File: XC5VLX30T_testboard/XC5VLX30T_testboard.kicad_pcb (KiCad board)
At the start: 4 copper layers, 19 parts, among them J1 Conn_01x35_Pin, J2 Conn_01x35_Pin, J3 Conn_01x35_Pin, J4 Conn_01x35_Pin, J5 Conn_01x35_Pin, J6 Conn_01x35_Pin, J7 Conn_01x35_Pin, J8 Conn_01x35_Pin, U1 XC5VLX30T-1FFG665C, X1 SG-5032CCN

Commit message: a
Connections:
- U1 pad AA16: unconnected-(U1F-IO_L4P_13-PadU26) -> VCCO
- U1 pad AA6: unconnected-(U1F-IO_L4P_13-PadU26) -> VCCO
- U1 pad AB13: unconnected-(U1F-IO_L4P_13-PadU26) -> VCCO
- U1 pad AB23: unconnected-(U1F-IO_L4P_13-PadU26) -> VCCO
- U1 pad AC10: unconnected-(U1F-IO_L4P_13-PadU26) -> VCCO
- U1 pad AC20: unconnected-(U1F-IO_L4P_13-PadU26) -> VCCO
- U1 pad B13: unconnected-(U1F-IO_L4P_13-PadU26) -> VCCO
- U1 pad B23: unconnected-(U1F-IO_L4P_13-PadU26) -> VCCO
- U1 pad C10: unconnected-(U1F-IO_L4P_13-PadU26) -> VCCO
- U1 pad C23: unconnected-(U1F-IO_L4P_13-PadU26) -> unconnected-(U1C-IO_L15N_15-PadC23)
- U1 pad D17: unconnected-(U1F-IO_L4P_13-PadU26) -> VCCO
- U1 pad D23: unconnected-(U1F-IO_L4P_13-PadU26) -> unconnected-(U1D-IO_L12P_VRN_15-PadD23)
- U1 pad D7: unconnected-(U1F-IO_L4P_13-PadU26) -> VCCO
- U1 pad E14: unconnected-(U1F-IO_L4P_13-PadU26) -> VCCO
- U1 pad E24: unconnected-(U1F-IO_L4P_13-PadU26) -> VCCO
- U1 pad F11: unconnected-(U1F-IO_L4P_13-PadU26) -> VCCO
- U1 pad F21: unconnected-(U1F-IO_L4P_13-PadU26) -> VCCO
- U1 pad G18: unconnected-(U1F-IO_L4P_13-PadU26) -> VCCO
- U1 pad G8: unconnected-(U1F-IO_L4P_13-PadU26) -> VCCO
- U1 pad H25: unconnected-(U1F-IO_L4P_13-PadU26) -> VCCO
- U1 pad H5: unconnected-(U1F-IO_L4P_13-PadU26) -> VCCO
- U1 pad H6: unconnected-(U1F-IO_L4P_13-PadU26) -> unconnected-(U1A-IO_L1N_12-PadH6)
- U1 pad J12: unconnected-(U1F-IO_L4P_13-PadU26) -> VCCO
- U1 pad J22: unconnected-(U1F-IO_L4P_13-PadU26) -> VCCO
- U1 pad J6: unconnected-(U1F-IO_L4P_13-PadU26) -> unconnected-(U1A-IO_L7N_12-PadJ6)
- U1 pad K6: unconnected-(U1F-IO_L4P_13-PadU26) -> unconnected-(U1A-IO_L10P_CC_12-PadK6)
- U1 pad L6: unconnected-(U1F-IO_L4P_13-PadU26) -> VCCO
- U1 pad M22: unconnected-(U1F-IO_L4P_13-PadU26) -> unconnected-(U1E-IO_L19N_SM9N_11-PadM22)
- U1 pad M23: unconnected-(U1F-IO_L4P_13-PadU26) -> VCCO
- U1 pad M7: unconnected-(U1F-IO_L4P_13-PadU26) -> unconnected-(U1B-IO_L14P_12-PadM7)
- U1 pad N23: unconnected-(U1F-IO_L4P_13-PadU26) -> VCCO
- U1 pad N7: unconnected-(U1F-IO_L4P_13-PadU26) -> unconnected-(U1B-IO_L17N_12-PadN7)
- U1 pad P23: unconnected-(U1F-IO_L4P_13-PadU26) -> VCCO
- U1 pad P7: unconnected-(U1F-IO_L4P_13-PadU26) -> VCCO
- U1 pad R23: unconnected-(U1F-IO_L4P_13-PadU26) -> unconnected-(U1E-IO_L3P_SM5P_13-PadR23)
- U1 pad R24: unconnected-(U1F-IO_L4P_13-PadU26) -> VCCO
- U1 pad R7: unconnected-(U1F-IO_L4P_13-PadU26) -> VCCO
- U1 pad T7: unconnected-(U1F-IO_L4P_13-PadU26) -> VCCO
- U1 pad V23: unconnected-(U1F-IO_L4P_13-PadU26) -> VCCO
- U1 pad V25: unconnected-(U1F-IO_L4P_13-PadU26) -> VCCO
- U1 pad W22: unconnected-(U1F-IO_L4P_13-PadU26) -> VCCO
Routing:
- net unconnected-(U1F-IO_L4P_13-PadU26): track 272.2 -> 22.3 mm, vias 43 -> 2
- net VCCO: track 2.83 -> 141.2 mm, vias 4 -> 42
- net unconnected-(U1C-IO_L15N_15-PadC23): track 0.00 -> 32.4 mm, vias 0 -> 3
- net unconnected-(U1E-IO_L19N_SM9N_11-PadM22): track 0.00 -> 28.0 mm, vias 0 -> 2
- net unconnected-(U1E-IO_L10P_CC_SM15P_11-PadL23): track 0.71 -> 28.0 mm
- net unconnected-(U1E-IO_L18P_SM10P_11-PadN24): track 7.72 -> 29.5 mm, vias 1 -> 2
- net unconnected-(U1E-IO_L3P_SM5P_13-PadR23): track 0.00 -> 20.5 mm, vias 0 -> 2
- net unconnected-(U1E-IO_L19P_SM9P_11-PadN22): track 10.4 -> 30.7 mm, vias 1 -> 2
- net unconnected-(U1A-IO_L7N_16-PadD6): track 30.4 -> 10.4 mm
- net unconnected-(U1D-IO_L16P_15-PadD24): track 7.35 -> 27.4 mm, vias 1 -> 2
- net unconnected-(U1E-IO_L1P_SM7P_13-PadP25): track 6.95 -> 26.2 mm
- net unconnected-(U1D-IO_L6N_11-PadH22): track 9.77 -> 28.7 mm, vias 1 -> 2
- net unconnected-(U1D-IO_L2P_11-PadH26): track 6.41 -> 25.2 mm, vias 0 -> 1
- net unconnected-(U1E-IO_L16P_SM12P_11-PadN26): track 8.27 -> 27.0 mm, vias 0 -> 1
- net unconnected-(U1E-IO_L0P_SM8P_13-PadP26): track 13.8 -> 32.2 mm, vias 1 -> 2
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- added copper zone on In1.Cu, net VCCO
- added copper zone on F.Cu, net VccINT

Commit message: via routing
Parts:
- moved C1 2.89 mm to (158.8, 127.7)
- moved C3 2.75 mm to (163.9, 127.8)
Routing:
- net unconnected-(U1A-IO_L18P_16-PadD5): track 10.8 -> 28.8 mm
- net unconnected-(U1A-IO_L18N_16-PadE5): track 11.2 -> 29.2 mm
- net unconnected-(U1A-IO_L3P_16-PadH8): track 9.07 -> 26.2 mm
- net unconnected-(U1A-IO_L3N_12-PadF5): track 11.8 -> 27.4 mm
- net unconnected-(U1A-IO_L7N_12-PadJ6): track 8.60 -> 22.8 mm
- net unconnected-(U1A-IO_L5P_12-PadG4): track 11.4 -> 25.2 mm
- net unconnected-(U1A-IO_L3P_12-PadG5): track 9.29 -> 21.0 mm
- net unconnected-(U1A-IO_L9P_CC_12-PadK5): track 8.89 -> 20.4 mm
- net unconnected-(U1A-IO_L7P_12-PadJ5): track 9.17 -> 20.6 mm
- net unconnected-(U1B-IO_L16N_12-PadN6): track 9.69 -> 20.8 mm
- net unconnected-(U1G-IO_L19N_17-PadAD14): track 4.35 -> 13.9 mm
- net unconnected-(U1B-IO_L17P_12-PadM6): track 9.92 -> 19.2 mm
- net unconnected-(U1G-IO_L7N_GC_VRP_4-PadAC14): track 5.27 -> 14.4 mm
- net unconnected-(U1C-IO_L17P_18-PadAC8): track 6.05 -> 15.1 mm
- net unconnected-(U1B-IO_L11N_CC_12-PadU5): track 7.74 -> 16.4 mm
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- added copper zone on F.Cu, net VCCO

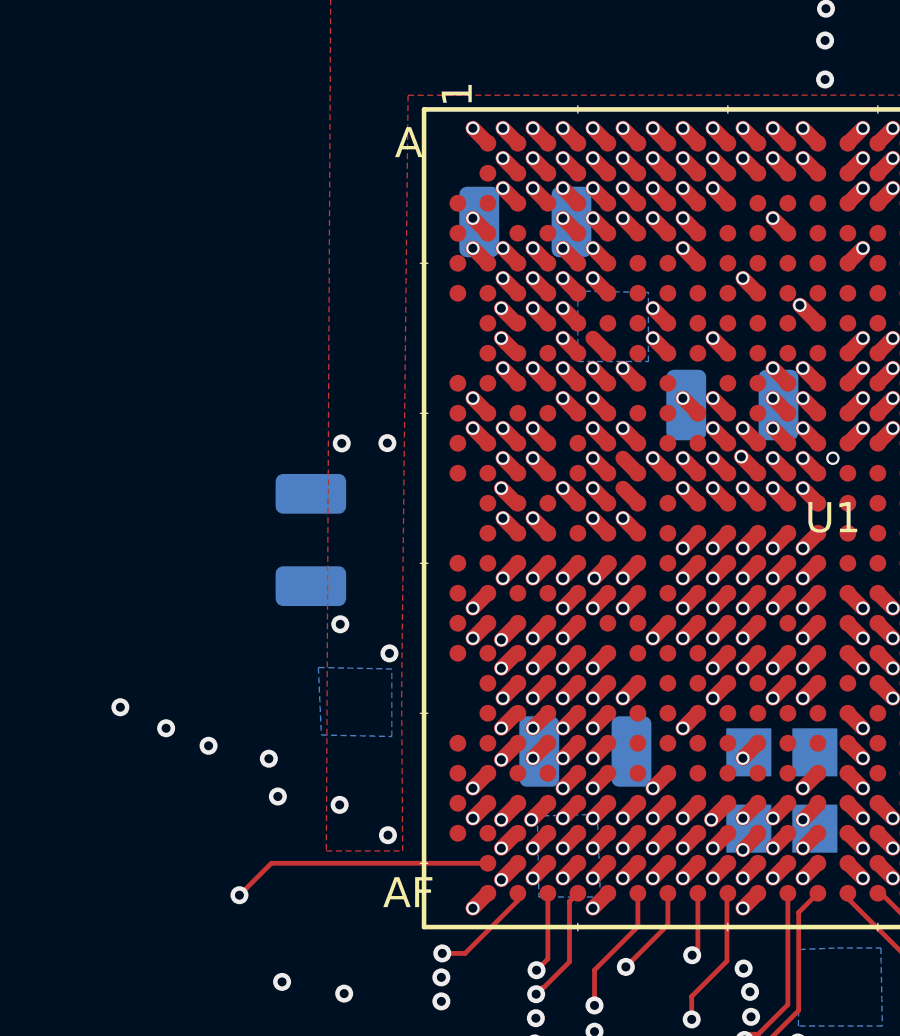
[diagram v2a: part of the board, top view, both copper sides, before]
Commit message: fixed missing pins
MGTRXP/MGTRXN wasnt connected to GND
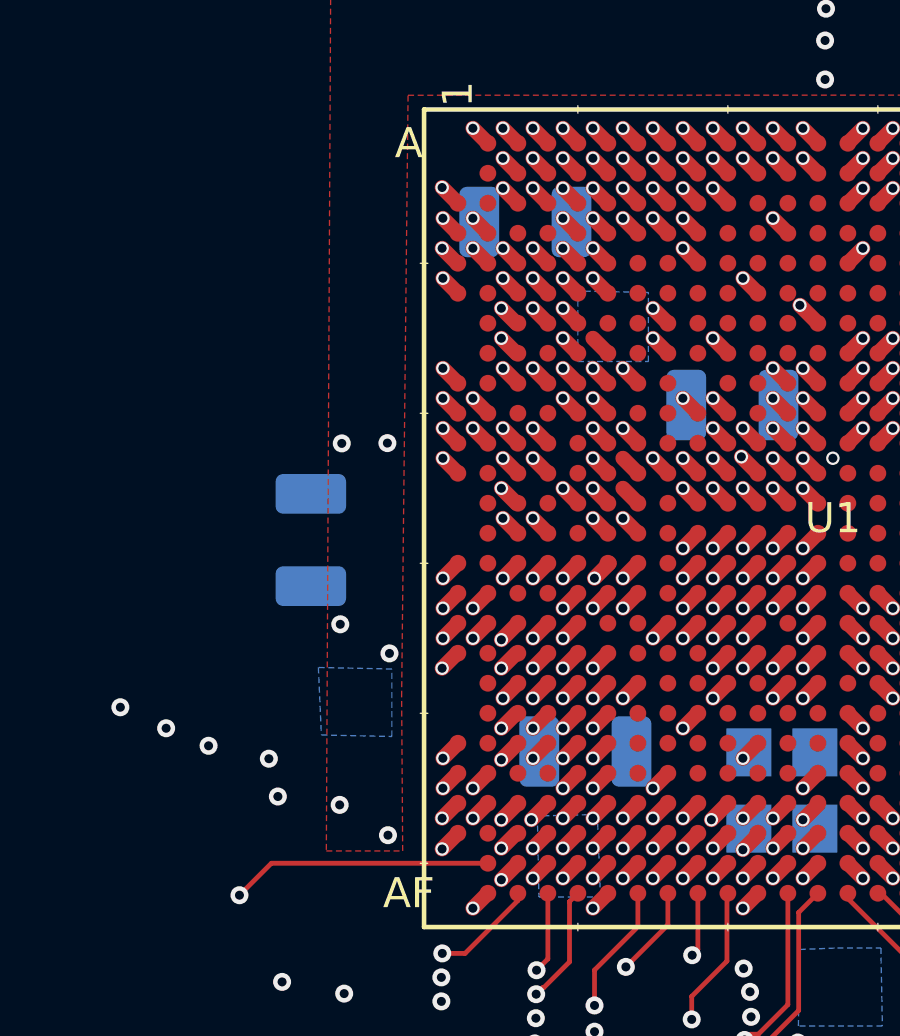
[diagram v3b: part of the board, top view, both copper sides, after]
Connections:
- U1 pad AA1: unconnected-(U1B-MGTRXP0_118-PadAA1) -> GND
- U1 pad AB1: unconnected-(U1C-MGTRXN0_118-PadAB1) -> GND
- U1 pad AC1: unconnected-(U1C-MGTRXN1_118-PadAC1) -> GND
- U1 pad AD1: unconnected-(U1C-MGTRXP1_118-PadAD1) -> GND
- U1 pad C1: unconnected-(U1A-MGTRXP0_116-PadC1) -> GND
- U1 pad D1: unconnected-(U1A-MGTRXN0_116-PadD1) -> GND
- U1 pad E1: unconnected-(U1A-MGTRXN1_116-PadE1) -> GND
- U1 pad F1: unconnected-(U1A-MGTRXP1_116-PadF1) -> GND
- U1 pad J1: unconnected-(U1A-MGTRXP0_112-PadJ1) -> GND
- U1 pad K1: unconnected-(U1A-MGTRXN0_112-PadK1) -> GND
- U1 pad L1: unconnected-(U1A-MGTRXN1_112-PadL1) -> GND
- U1 pad M1: unconnected-(U1A-MGTRXP1_112-PadM1) -> GND
- U1 pad N23: VCCO -> unconnected-(U1E-IO_L18N_SM10N_11-PadN23)
- U1 pad P23: VCCO -> unconnected-(U1E-IO_L2N_SM6N_13-PadP23)
- U1 pad R1: unconnected-(U1B-MGTRXP0_114-PadR1) -> GND
- U1 pad R7: VCCO -> unconnected-(U1B-IO_L19N_12-PadR7)
- U1 pad T1: unconnected-(U1B-MGTRXN0_114-PadT1) -> GND
- U1 pad T7: VCCO -> unconnected-(U1B-IO_L15N_12-PadT7)
- U1 pad U1: unconnected-(U1B-MGTRXN1_114-PadU1) -> GND
- U1 pad V1: unconnected-(U1B-MGTRXP1_114-PadV1) -> GND
- U1 pad V23: VCCO -> unconnected-(U1F-IO_L9N_CC_SM0N_13-PadV23)
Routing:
- net GND: track 101.8 -> 113.1 mm, vias 144 -> 160

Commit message: more routing
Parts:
- moved X1 21.9 mm to (148.8, 173.1)
- moved C4 21.4 mm to (175.6, 177.3)
- moved C8 15.2 mm to (146.5, 166.6)
- moved C7 10.4 mm to (136.7, 148.8)
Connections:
- J1 pad 1: unconnected-(J1-Pin_1-Pad1) -> GND
- J1 pad 14: unconnected-(J1-Pin_14-Pad14) -> GND
- J1 pad 21: unconnected-(J1-Pin_21-Pad21) -> GND
- J1 pad 28: unconnected-(J1-Pin_28-Pad28) -> GND
- J1 pad 35: unconnected-(J1-Pin_35-Pad35) -> GND
- J1 pad 7: unconnected-(J1-Pin_7-Pad7) -> GND
- J2 pad 1: unconnected-(J2-Pin_1-Pad1) -> GND
- J2 pad 14: unconnected-(J2-Pin_14-Pad14) -> GND
- J2 pad 21: unconnected-(J2-Pin_21-Pad21) -> GND
- J2 pad 28: unconnected-(J2-Pin_28-Pad28) -> GND
- J2 pad 35: unconnected-(J2-Pin_35-Pad35) -> GND
- J2 pad 7: unconnected-(J2-Pin_7-Pad7) -> GND
- J3 pad 1: unconnected-(J3-Pin_1-Pad1) -> GND
- J3 pad 14: unconnected-(J3-Pin_14-Pad14) -> GND
- J3 pad 2: J5PIN1 -> IO_L7P_16
- J3 pad 21: unconnected-(J3-Pin_21-Pad21) -> GND
- J3 pad 28: unconnected-(J3-Pin_28-Pad28) -> GND
- J3 pad 3: J5PIN1 -> IO_L14N_VREF_16
- J3 pad 35: unconnected-(J3-Pin_35-Pad35) -> GND
- J3 pad 4: J5PIN1 -> IO_L16P_16
- J3 pad 7: unconnected-(J3-Pin_7-Pad7) -> GND
- J4 pad 1: unconnected-(J4-Pin_1-Pad1) -> GND
- J4 pad 14: unconnected-(J4-Pin_14-Pad14) -> GND
- J4 pad 21: unconnected-(J4-Pin_21-Pad21) -> GND
- J4 pad 28: unconnected-(J4-Pin_28-Pad28) -> GND
- J4 pad 35: unconnected-(J4-Pin_35-Pad35) -> GND
- J4 pad 7: unconnected-(J4-Pin_7-Pad7) -> GND
- J5 pad 1: J5PIN1 -> GND
- J5 pad 14: unconnected-(J5-Pin_14-Pad14) -> GND
- J5 pad 21: unconnected-(J5-Pin_21-Pad21) -> GND
- J5 pad 28: unconnected-(J5-Pin_28-Pad28) -> GND
- J5 pad 35: unconnected-(J5-Pin_35-Pad35) -> GND
- J5 pad 7: unconnected-(J5-Pin_7-Pad7) -> GND
- J6 pad 1: unconnected-(J6-Pin_1-Pad1) -> GND
- J6 pad 14: unconnected-(J6-Pin_14-Pad14) -> GND
- J6 pad 21: unconnected-(J6-Pin_21-Pad21) -> GND
- J6 pad 28: unconnected-(J6-Pin_28-Pad28) -> GND
- J6 pad 35: unconnected-(J6-Pin_35-Pad35) -> GND
- J6 pad 7: unconnected-(J6-Pin_7-Pad7) -> GND
- J7 pad 1: unconnected-(J7-Pin_1-Pad1) -> GND
- J7 pad 14: unconnected-(J7-Pin_14-Pad14) -> GND
- J7 pad 21: unconnected-(J7-Pin_21-Pad21) -> GND
- J7 pad 28: unconnected-(J7-Pin_28-Pad28) -> GND
- J7 pad 35: unconnected-(J7-Pin_35-Pad35) -> GND
- J7 pad 7: unconnected-(J7-Pin_7-Pad7) -> GND
- J8 pad 1: unconnected-(J8-Pin_1-Pad1) -> GND
- J8 pad 14: unconnected-(J8-Pin_14-Pad14) -> GND
- J8 pad 21: unconnected-(J8-Pin_21-Pad21) -> GND
- J8 pad 28: unconnected-(J8-Pin_28-Pad28) -> GND
- J8 pad 35: unconnected-(J8-Pin_35-Pad35) -> GND
- J8 pad 7: unconnected-(J8-Pin_7-Pad7) -> GND
- U1 pad A10: unconnected-(U1B-IO_L13N_16-PadA10) -> IO_L13N_16
- U1 pad A12: unconnected-(U1B-IO_L15N_16-PadA12) -> IO_L15N_16
- U1 pad A13: unconnected-(U1B-IO_L1N_15-PadA13) -> IO_L1N_15
- U1 pad A14: unconnected-(U1B-IO_L2P_15-PadA14) -> IO_L2P_15
- U1 pad A15: unconnected-(U1B-IO_L2N_15-PadA15) -> IO_L2N_15
- U1 pad A17: unconnected-(U1B-IO_L5N_15-PadA17) -> IO_L5N_15
- U1 pad A18: unconnected-(U1B-IO_L6P_15-PadA18) -> IO_L6P_15
- U1 pad A19: unconnected-(U1B-IO_L6N_15-PadA19) -> IO_L6N_15
- U1 pad A20: unconnected-(U1B-IO_L8P_CC_15-PadA20) -> IO_L8P_CC_15
- U1 pad A22: unconnected-(U1B-IO_L13N_15-PadA22) -> IO_L13N_15
- U1 pad A23: unconnected-(U1B-IO_L14P_15-PadA23) -> IO_L14P_15
- U1 pad A24: unconnected-(U1B-IO_L14N_VREF_15-PadA24) -> IO_L14N_VREF_15
- U1 pad A25: unconnected-(U1B-IO_L17N_15-PadA25) -> IO_L17N_15
- U1 pad A3: unconnected-(U1A-IO_L14N_VREF_16-PadA3) -> IO_L14N_VREF_16
- U1 pad A5: unconnected-(U1A-IO_L12N_VRP_16-PadA5) -> IO_L12N_VRP_16
- U1 pad A7: unconnected-(U1A-IO_L10P_CC_16-PadA7) -> IO_L10P_CC_16
- U1 pad A8: unconnected-(U1A-IO_L4N_VREF_16-PadA8) -> IO_L4N_VREF_16
- U1 pad A9: unconnected-(U1A-IO_L4P_16-PadA9) -> IO_L4P_16
- U1 pad AA14: unconnected-(U1F-IO_L6N_D6_2-PadAA14) -> IO_L6N_D6_2
- U1 pad AA24: unconnected-(U1G-IO_L14N_VREF_13-PadAA24) -> IO_L14N_VREF_13
- U1 pad AA25: unconnected-(U1G-IO_L13P_13-PadAA25) -> IO_L13P_13
- U1 pad AA5: unconnected-(U1C-IO_L9P_CC_18-PadAA5) -> IO_L9P_CC_18
- U1 pad AB14: unconnected-(U1G-IO_L7P_GC_VRN_4-PadAB14) -> IO_L7P_GC_VRN_4
- U1 pad AB24: unconnected-(U1G-IO_L15P_13-PadAB24) -> IO_L15P_13
- U1 pad AB25: unconnected-(U1G-IO_L14P_13-PadAB25) -> IO_L14P_13
- U1 pad AB26: unconnected-(U1G-IO_L13N_13-PadAB26) -> IO_L13N_13
- U1 pad AB5: unconnected-(U1C-IO_L9N_CC_18-PadAB5) -> IO_L9N_CC_18
- U1 pad AB6: unconnected-(U1C-IO_L10P_CC_18-PadAB6) -> IO_L10P_CC_18
- U1 pad AB7: unconnected-(U1C-IO_L10N_CC_18-PadAB7) -> IO_L10N_CC_18
- U1 pad AB9: unconnected-(U1C-IO_L19P_18-PadAB9) -> IO_L19P_18
- U1 pad AC11: unconnected-(U1G-IO_L3P_GC_D9_4-PadAC11) -> IO_L3P_GC_D9_4
- U1 pad AC12: unconnected-(U1G-IO_L5P_GC_4-PadAC12) -> IO_L5P_GC_4
- U1 pad AC13: unconnected-(U1G-IO_L5N_GC_4-PadAC13) -> IO_L5N_GC_4
- U1 pad AC14: unconnected-(U1G-IO_L7N_GC_VRP_4-PadAC14) -> IO_L7N_GC_VRP
- U1 pad AC17: unconnected-(U1G-IO_L8P_CC_GC_4-PadAC17) -> IO_L8P_CC_GC_4
- U1 pad AC18: unconnected-(U1G-IO_L6P_GC_4-PadAC18) -> IO_L6P_GC_4
- U1 pad AC19: unconnected-(U1G-IO_L4N_GC_VREF_4-PadAC19) -> IO_L4N_GC_VREF_4
- U1 pad AC21: unconnected-(U1G-IO_L11P_CC_17-PadAC21) -> IO_L11P_CC_17
- U1 pad AC22: unconnected-(U1G-IO_L7P_17-PadAC22) -> IO_L7P_17
- U1 pad AC23: unconnected-(U1G-IO_L6N_17-PadAC23) -> IO_L6N_17
- U1 pad AC24: unconnected-(U1G-IO_L6P_17-PadAC24) -> IO_L6P_17
- U1 pad AC26: unconnected-(U1G-IO_L0P_17-PadAC26) -> IO_L0P_17
- U1 pad AC6: unconnected-(U1C-IO_L12P_VRN_18-PadAC6) -> IO_L12P_VRN_18
- U1 pad AC7: unconnected-(U1C-IO_L16N_18-PadAC7) -> IO_L16N_18
- U1 pad AC8: unconnected-(U1C-IO_L17P_18-PadAC8) -> IO_L17N_18
- U1 pad AC9: unconnected-(U1C-IO_L18N_18-PadAC9) -> IO_L18N_18
- U1 pad AD10: unconnected-(U1G-IO_L4P_18-PadAD10) -> IO_L4P_18
- U1 pad AD11: unconnected-(U1G-IO_L2N_18-PadAD11) -> IO_L2N_18
- U1 pad AD13: unconnected-(U1G-IO_L19P_17-PadAD13) -> IO_L19P_17
- U1 pad AD14: unconnected-(U1G-IO_L19N_17-PadAD14) -> IO_L19N_17
- U1 pad AD15: unconnected-(U1G-IO_L16P_17-PadAD15) -> IO_L16P_17
- U1 pad AD16: unconnected-(U1G-IO_L15N_17-PadAD16) -> IO_L15N_17
- U1 pad AD18: unconnected-(U1G-IO_L13N_17-PadAD18) -> IO_L13N_17
- U1 pad AD19: unconnected-(U1G-IO_L10P_CC_17-PadAD19) -> IO_L10P_CC_17
- U1 pad AD20: unconnected-(U1G-IO_L10N_CC_17-PadAD20) -> IO_L10N_CC_17
- U1 pad AD21: unconnected-(U1G-IO_L11N_CC_17-PadAD21) -> IO_L11N_CC_17
- U1 pad AD23: unconnected-(U1G-IO_L5N_17-PadAD23) -> IO_L5N_17
- U1 pad AD24: unconnected-(U1G-IO_L1N_17-PadAD24) -> IO_L1N_17
- U1 pad AD25: unconnected-(U1G-IO_L1P_17-PadAD25) -> IO_L1P_17
- U1 pad AD26: unconnected-(U1G-IO_L0N_17-PadAD26) -> IO_L0N_17
- U1 pad AD4: unconnected-(U1C-IO_L14N_VREF_18-PadAD4) -> IO_L14N_VREF_18
- U1 pad AD5: unconnected-(U1C-IO_L12N_VRP_18-PadAD5) -> IO_L12N_VRP_18
- U1 pad AD6: unconnected-(U1C-IO_L16P_18-PadAD6) -> IO_L16P_18
- U1 pad AD8: unconnected-(U1C-IO_L17N_18-PadAD8) -> IO_L17N_18
- U1 pad AD9: unconnected-(U1C-IO_L18P_18-PadAD9) -> IO_L18P_18
- U1 pad B10: unconnected-(U1C-IO_L13P_16-PadB10) -> IO_L13P_16
- U1 pad B11: unconnected-(U1C-IO_L15P_16-PadB11) -> IO_L15P_16
- U1 pad B12: unconnected-(U1C-IO_L17P_16-PadB12) -> IO_L17P_16
- U1 pad B14: unconnected-(U1C-IO_L1P_15-PadB14) -> IO_L1P_15
- U1 pad B15: unconnected-(U1C-IO_L3P_15-PadB15) -> IO_L3P_15
- U1 pad B16: unconnected-(U1C-IO_L4P_15-PadB16) -> IO_L4P_15
- U1 pad B17: unconnected-(U1C-IO_L5P_15-PadB17) -> IO_L5P_15
- U1 pad B19: unconnected-(U1C-IO_L7P_15-PadB19) -> IO_L7P_15
- U1 pad B20: unconnected-(U1C-IO_L8N_CC_15-PadB20) -> IO_L8N_CC_15
- U1 pad B21: unconnected-(U1C-IO_L11P_CC_15-PadB21) -> IO_L11P_CC_15
- U1 pad B22: unconnected-(U1C-IO_L13P_15-PadB22) -> IO_L13P_15
- U1 pad B24: unconnected-(U1C-IO_L15P_15-PadB24) -> IO_L13P_15
- U1 pad B25: unconnected-(U1C-IO_L17P_15-PadB25) -> IO_L17P_15
- U1 pad B26: unconnected-(U1C-IO_L18P_15-PadB26) -> IO_L18P_15
- U1 pad B5: unconnected-(U1A-IO_L16N_16-PadB5) -> IO_L16N_16
- U1 pad B6: unconnected-(U1A-IO_L12P_VRN_16-PadB6) -> IO_L12P_VRN_16
- U1 pad B7: unconnected-(U1A-IO_L10N_CC_16-PadB7) -> IO_L10N_CC_16
- U1 pad B9: unconnected-(U1A-IO_L6P_16-PadB9) -> IO_L6P_16
- U1 pad C13: unconnected-(U1C-IO_L0P_15-PadC13) -> IO_L0P_15
- U1 pad C14: unconnected-(U1C-IO_L0N_15-PadC14) -> IO_L0N_15
- U1 pad C18: unconnected-(U1C-IO_L7N_15-PadC18) -> IO_L7N_15
- U1 pad C21: unconnected-(U1C-IO_L11N_CC_15-PadC21) -> IO_L11N_CC_15
- U1 pad C22: unconnected-(U1C-IO_L12N_VRP_15-PadC22) -> IO_L12N_VRP_15
- U1 pad C23: unconnected-(U1C-IO_L15N_15-PadC23) -> IO_L15N_15
- U1 pad C24: unconnected-(U1C-IO_L16N_15-PadC24) -> IO_L16N_15
- U1 pad C26: unconnected-(U1C-IO_L18N_15-PadC26) -> IO_L18N_15
- U1 pad C6: unconnected-(U1A-IO_L9N_CC_16-PadC6) -> IO_L9N_CC_16
- U1 pad C7: unconnected-(U1A-IO_L9P_CC_16-PadC7) -> IO_L9P_CC_16
- U1 pad C8: unconnected-(U1A-IO_L6N_16-PadC8) -> IO_L6N_16
- U1 pad C9: unconnected-(U1A-IO_L8P_CC_16-PadC9) -> IO_L8P_CC_16
- U1 pad D21: unconnected-(U1D-IO_L10P_CC_15-PadD21) -> IO_L10P_CC_15
- U1 pad D23: unconnected-(U1D-IO_L12P_VRN_15-PadD23) -> IO_L12P_VRN_15
- U1 pad D24: unconnected-(U1D-IO_L16P_15-PadD24) -> IO_L16N_15
- U1 pad D25: unconnected-(U1D-IO_L19N_15-PadD25) -> IO_L19N_15
- U1 pad D26: unconnected-(U1D-IO_L19P_15-PadD26) -> IO_L19P_15
- U1 pad D5: unconnected-(U1A-IO_L18P_16-PadD5) -> IO_L18P_16
- U1 pad D6: unconnected-(U1A-IO_L7N_16-PadD6) -> IO_L7N_16
- U1 pad D8: unconnected-(U1A-IO_L8N_CC_16-PadD8) -> IO_L8N_CC_16
- U1 pad D9: unconnected-(U1A-IO_L11P_CC_16-PadD9) -> IO_L11P_CC_16
- U1 pad E23: unconnected-(U1D-IO_L4P_11-PadE23) -> IO_L4P_11
- U1 pad E25: unconnected-(U1D-IO_L0N_11-PadE25) -> IO_L0N_11
- U1 pad E26: unconnected-(U1D-IO_L0P_11-PadE26) -> IO_L0P_11
- U1 pad E5: unconnected-(U1A-IO_L18N_16-PadE5) -> IO_L18N_16
- U1 pad F24: unconnected-(U1D-IO_L3P_11-PadF24) -> IO_L3P_11
- U1 pad F25: unconnected-(U1D-IO_L1P_11-PadF25) -> IO_L1P_11
- U1 pad F5: unconnected-(U1A-IO_L3N_12-PadF5) -> IO_L7P_16
- U1 pad G22: unconnected-(U1D-IO_L6P_11-PadG22) -> IO_L6P_11
- U1 pad G24: unconnected-(U1D-IO_L3N_11-PadG24) -> IO_L3N_11
- U1 pad G25: unconnected-(U1D-IO_L2N_11-PadG25) -> IO_L2N_11
- U1 pad G26: unconnected-(U1D-IO_L1N_11-PadG26) -> IO_L1N_11
- U1 pad G4: unconnected-(U1A-IO_L5P_12-PadG4) -> IO_L5P_12
- U1 pad G5: unconnected-(U1A-IO_L3P_12-PadG5) -> IO_L3P_12
- U1 pad G6: unconnected-(U1A-IO_L1P_12-PadG6) -> IO_L1P_12
- U1 pad H22: unconnected-(U1D-IO_L6N_11-PadH22) -> IO_L6N_11
- U1 pad H4: unconnected-(U1A-IO_L5N_12-PadH4) -> IO_L5N_12
- U1 pad J23: unconnected-(U1D-IO_L7N_11-PadJ23) -> IO_L7N_11
- U1 pad J24: unconnected-(U1D-IO_L12N_VRP_11-PadJ24) -> IO_L12N_VRP_11
- U1 pad J25: unconnected-(U1D-IO_L13P_11-PadJ25) -> IO_L13P_11
- U1 pad J26: unconnected-(U1D-IO_L13N_11-PadJ26) -> IO_L13N_11
- U1 pad J5: unconnected-(U1A-IO_L7P_12-PadJ5) -> IO_L7P_12
- U1 pad J6: unconnected-(U1A-IO_L7N_12-PadJ6) -> IO_L7N_12
- U1 pad K22: unconnected-(U1E-IO_L9P_CC_11-PadK22) -> IO_L9P_CC_11
- U1 pad K23: unconnected-(U1E-IO_L9N_CC_11-PadK23) -> IO_L9N_CC_11
- U1 pad K25: unconnected-(U1E-IO_L15N_SM13N_11-PadK25) -> IO_L15N_SM13N_11
- U1 pad K26: unconnected-(U1E-IO_L14P_11-PadK26) -> IO_L14P_11
- U1 pad K5: unconnected-(U1A-IO_L9P_CC_12-PadK5) -> IO_L9P_CC_12
- U1 pad K6: unconnected-(U1A-IO_L10P_CC_12-PadK6) -> IO_L10P_CC_12
- U1 pad L22: unconnected-(U1E-IO_L10N_CC_SM15N_11-PadL22) -> IO_L10N_CC_SM15N_11
- U1 pad L23: unconnected-(U1E-IO_L10P_CC_SM15P_11-PadL23) -> IO_L10P_CC_SM15P_11
- U1 pad L24: unconnected-(U1E-IO_L15P_SM13P_11-PadL24) -> IO_L15P_CC_SM13P_11
- U1 pad L5: unconnected-(U1A-IO_L9N_CC_12-PadL5) -> IO_L9N_CC_12
- U1 pad M22: unconnected-(U1E-IO_L19N_SM9N_11-PadM22) -> IO_L19N_SM9N_11
- U1 pad M24: unconnected-(U1E-IO_L17N_SM11N_11-PadM24) -> IO_L17N_SM11N_11
- U1 pad M25: unconnected-(U1E-IO_L17P_SM11P_11-PadM25) -> IO_L17P_SM11P_11
- U1 pad M26: unconnected-(U1E-IO_L16N_SM12N_11-PadM26) -> IO_L16N_SM12N_11
- U1 pad M6: unconnected-(U1B-IO_L17P_12-PadM6) -> IO_L17P_12
- U1 pad N22: unconnected-(U1E-IO_L19P_SM9P_11-PadN22) -> IO_L19P_SM9P_11
- U1 pad N23: unconnected-(U1E-IO_L18N_SM10N_11-PadN23) -> IO_L18N_SM10N_11
- U1 pad N24: unconnected-(U1E-IO_L18P_SM10P_11-PadN24) -> IO_L18P_SM10P_11
- U1 pad P23: unconnected-(U1E-IO_L2N_SM6N_13-PadP23) -> IO_L2N_SM6N_13
- U1 pad P24: unconnected-(U1E-IO_L2P_SM6P_13-PadP24) -> IO_L2P_SM6P_13
- U1 pad P25: unconnected-(U1E-IO_L1P_SM7P_13-PadP25) -> IO_L1P_SM7P_13
- U1 pad P26: unconnected-(U1E-IO_L0P_SM8P_13-PadP26) -> IO_L0P_SM8P_13
- U1 pad R22: unconnected-(U1E-IO_L3N_SM5N_13-PadR22) -> IO_L3N_SM5N_13
- U1 pad R23: unconnected-(U1E-IO_L3P_SM5P_13-PadR23) -> IO_L3P_SM5P_13
- U1 pad R25: unconnected-(U1F-IO_L1N_SM7N_13-PadR25) -> IO_L1N_SM7N_13
- U1 pad R26: unconnected-(U1F-IO_L0N_SM8N_13-PadR26) -> IO_L0N_SM8N_13
- U1 pad R5: unconnected-(U1B-IO_L13N_12-PadR5) -> IO_L13_N_12
- U1 pad R6: unconnected-(U1B-IO_L15P_12-PadR6) -> IO_L15_N_12
- U1 pad R7: unconnected-(U1B-IO_L19N_12-PadR7) -> IO_L19_N_12
- U1 pad T24: unconnected-(U1F-IO_L6P_SM3P_13-PadT24) -> IO_L6P_SM3P_13
- U1 pad T25: unconnected-(U1F-IO_L5N_SM4N_13-PadT25) -> IO_L5N_SM4N_13
- U1 pad T5: unconnected-(U1B-IO_L13P_12-PadT5) -> IO_L13P_12
- U1 pad T7: unconnected-(U1B-IO_L15N_12-PadT7) -> IO_L15N_12
- U1 pad U25: unconnected-(U1F-IO_L5P_SM4P_13-PadU25) -> IO_L5P_SM4P_13
- U1 pad U26: unconnected-(U1F-IO_L4P_13-PadU26) -> IO_L4P_13
- U1 pad U5: unconnected-(U1B-IO_L11N_CC_12-PadU5) -> IO_L11N_CC_12
- U1 pad V24: unconnected-(U1F-IO_L7N_SM2N_13-PadV24) -> IO_L7N_SM2N_13
- U1 pad V26: unconnected-(U1F-IO_L4N_VREF_13-PadV26) -> IO_L4N_VREF_13
- U1 pad V6: unconnected-(U1B-IO_L6P_12-PadV6) -> IO_L6P_12
- U1 pad W23: unconnected-(U1F-IO_L11N_CC_13-PadW23) -> IO_L11N_CC_13
- U1 pad W24: unconnected-(U1F-IO_L9P_CC_SM0P_13-PadW24) -> IO_L9P_CC_SM0P_13
- U1 pad W25: unconnected-(U1F-IO_L8N_CC_SM1N_13-PadW25) -> IO_L8N_CC_SM1N_13
- U1 pad W26: unconnected-(U1F-IO_L8P_CC_SM1P_13-PadW26) -> IO_L8P_CC_SM1P_13
- U1 pad W4: unconnected-(U1B-IO_L2N_12-PadW4) -> IO_L2N_12
- U1 pad W5: unconnected-(U1B-IO_L4P_12-PadW5) -> IO_L4P_12
- U1 pad W6: unconnected-(U1B-IO_L4N_VREF_12-PadW6) -> IO_L4N_VREF_12
- U1 pad Y25: unconnected-(U1F-IO_L12N_VRP_13-PadY25) -> IO_L12N_VRP_13
- U1 pad Y26: unconnected-(U1F-IO_L12P_VRN_13-PadY26) -> IO_L12P_VRN_13
- U1 pad Y4: unconnected-(U1B-IO_L2P_12-PadY4) -> IO_L2P_12
- U1 pad Y5: unconnected-(U1B-IO_L0N_12-PadY5) -> IO_L0N_12
- U1 pad Y6: unconnected-(U1B-IO_L0P_12-PadY6) -> IO_L0P_12
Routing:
- net (no net): track 0.00 -> 177.6 mm, vias 0 -> 1
- net GND: track 113.1 -> 184.2 mm, vias 160 -> 166
- net IO_L16N_15: track 0.00 -> 50.5 mm, vias 0 -> 3
- net IO_L14N_VREF_16: track 0.00 -> 46.5 mm, vias 0 -> 3
- net IO_L7P_16: track 35.9 -> 80.6 mm, vias 2 -> 4
- net unconnected-(U1A-IO_L10N_CC_16-PadB7): track 42.2 -> 0.00 mm, vias 1 -> 0
- net J5PIN1: track 39.5 -> 0.00 mm, vias 3 -> 0
- net IO_L16N_16: track 0.00 -> 33.6 mm, vias 0 -> 2
- net unconnected-(U1C-IO_L15N_15-PadC23): track 32.4 -> 0.00 mm, vias 3 -> 0
- net unconnected-(U1E-IO_L0P_SM8P_13-PadP26): track 32.2 -> 0.00 mm, vias 2 -> 0
- net IO_L0P_SM8P_13: track 0.00 -> 32.2 mm, vias 0 -> 2
- net unconnected-(U1B-IO_L2P_15-PadA14): track 31.9 -> 0.00 mm, vias 1 -> 0
- net IO_L2P_15: track 0.00 -> 31.9 mm, vias 0 -> 1
- net unconnected-(U1C-IO_L1P_15-PadB14): track 31.4 -> 0.00 mm, vias 1 -> 0
- net IO_L1P_15: track 0.00 -> 31.4 mm, vias 0 -> 1
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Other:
- board text removed: "VCCAUX"

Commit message: fixed DRC check errors
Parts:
- moved C2 31.9 mm to (171.0, 113.0)
- moved C15 21.1 mm to (190.9, 165.0)
- moved C13 15.6 mm to (170.4, 117.8)
- moved C12 15.0 mm to (143.0, 127.1)
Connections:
- U1 pad AC5: GND -> IO_L10P_CC_18
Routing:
- net GND: track 184.2 -> 157.7 mm, vias 166 -> 162
- net IO_L10P_CC_18: track 0.00 -> 15.5 mm, vias 0 -> 2
- net IO_L9P_CC_18: track 0.00 -> 11.1 mm, vias 0 -> 1
- net IO_L13P_15: track 28.6 -> 21.7 mm
- net IO_L15P_13: track 5.30 -> 11.9 mm
- net IO_L6P_17: track 9.65 -> 11.7 mm
- net VCCO: track 127.6 -> 126.3 mm
- removed copper zone on B.Cu, net CLK
- removed copper zone on B.Cu, net VCCO
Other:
- board text removed: "33 i/o"
- board text removed: "49 i/o"
- board text removed: "70 i/o"
- board text removed: "72 i/o"

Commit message: routing
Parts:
- moved C8 53.0 mm to (94.1, 174.8)
- moved X1 53.0 mm to (96.4, 181.3)
- moved C15 50.1 mm to (240.9, 168.1)
- moved C1 47.2 mm to (141.5, 83.8)
- moved C3 40.2 mm to (179.4, 90.7)
- moved C12 35.3 mm to (108.3, 120.7)
- moved C7 33.1 mm to (103.9, 144.2)
- moved C13 28.4 mm to (163.4, 90.4)
- moved C2 28.4 mm to (164.0, 85.5)
- moved C4 23.3 mm to (174.0, 200.6)
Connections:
- U1 pad AC5: IO_L10P_CC_18 -> GND
- U1 pad B24: IO_L13P_15 -> IO_L15P_15
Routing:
- net (no net): track 177.6 -> 0.00 mm, vias 1 -> 0
- net IO_L0P_17: track 13.0 -> 94.0 mm, vias 2 -> 4
- net IO_L17N_18: track 23.6 -> 103.5 mm, vias 3 -> 4
- net IO_L12N_VRP_18: track 22.3 -> 78.1 mm, vias 2 -> 3
- net IO_L4P_17: track 3.51 -> 54.8 mm, vias 1 -> 2
- net IO_L9N_CC_18: track 21.1 -> 72.3 mm, vias 2 -> 3
- net IO_L6P_18: track 2.14 -> 52.3 mm, vias 1 -> 2
- net IO_L17N_17: track 3.88 -> 52.3 mm, vias 1 -> 2
- net IO_L15P_15: track 0.00 -> 48.0 mm, vias 0 -> 2
- net IO_L12N_VRP_13: track 8.15 -> 55.6 mm, vias 1 -> 2
- net IO_L4N_VREF_18: track 7.59 -> 55.0 mm
- net IO_L3P_GC_D9_4: track 11.5 -> 58.8 mm, vias 1 -> 2
- net IO_L17P_12: track 19.6 -> 66.9 mm, vias 1 -> 2
- net IO_L12P_VRN_13: track 7.06 -> 54.2 mm, vias 1 -> 2
- net IO_L2P_18: track 5.33 -> 52.2 mm
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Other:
- board text removed: "VCCO"

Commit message: more routing
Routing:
- net IO_L18N_15: track 45.6 -> 3.93 mm, vias 2 -> 3
- net IO_L8P_CC_SM1P_13: track 62.1 -> 20.8 mm, vias 2 -> 3
- net IO_L0P_SM8P_13: track 46.8 -> 18.8 mm, vias 2 -> 3
- net IO_L17P_12: track 66.9 -> 43.3 mm
- net IO_L4P_17: track 54.8 -> 36.6 mm
- net IO_L17N_17: track 52.3 -> 42.0 mm
- net IO_L4P_13: track 55.9 -> 45.8 mm, vias 2 -> 3
- net IO_L10P_CC_SM15P_11: track 49.4 -> 40.4 mm
- net IO_L14N_VREF_11: track 45.5 -> 36.9 mm
- net IO_L0N_SM8N_13: track 49.5 -> 41.2 mm, vias 2 -> 3
- net unconnected-(U1E-IO_L16P_SM12P_11-PadN26): track 47.1 -> 38.8 mm
- net IO_L19N_SM9N_11: track 46.8 -> 40.0 mm
- net IO_L17N_SM11N_11: track 44.9 -> 38.2 mm
- net unconnected-(U1D-IO_L2P_11-PadH26): track 42.1 -> 36.8 mm, vias 1 -> 2
- net IO_L8P_CC_17: track 39.0 -> 33.9 mm
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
